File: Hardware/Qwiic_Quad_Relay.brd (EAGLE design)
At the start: 82.5 x 47 mm, 119 parts, among them J2 Qwiic Right Angle, J3 Qwiic Right Angle, J4 AVR_SPI_PROG_3X2TESTPOINTS, J9 POWER_JACK, K1 RELAY-SPDT-JZC-11F, K2 RELAY-SPDT-JZC-11F, K3 RELAY-SPDT-JZC-11F, K4 RELAY-SPDT-JZC-11F, Q1 600mA/40V, Q2 600mA/40V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

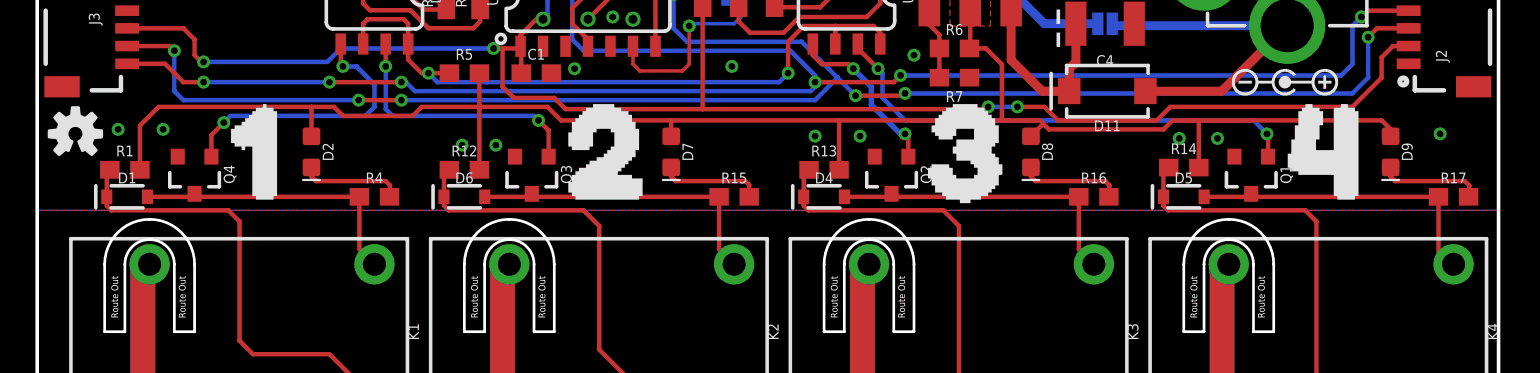
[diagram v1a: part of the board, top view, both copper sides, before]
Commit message: Moves 33 Ohm resistor to after the coil so that drop doesn't occur before it.
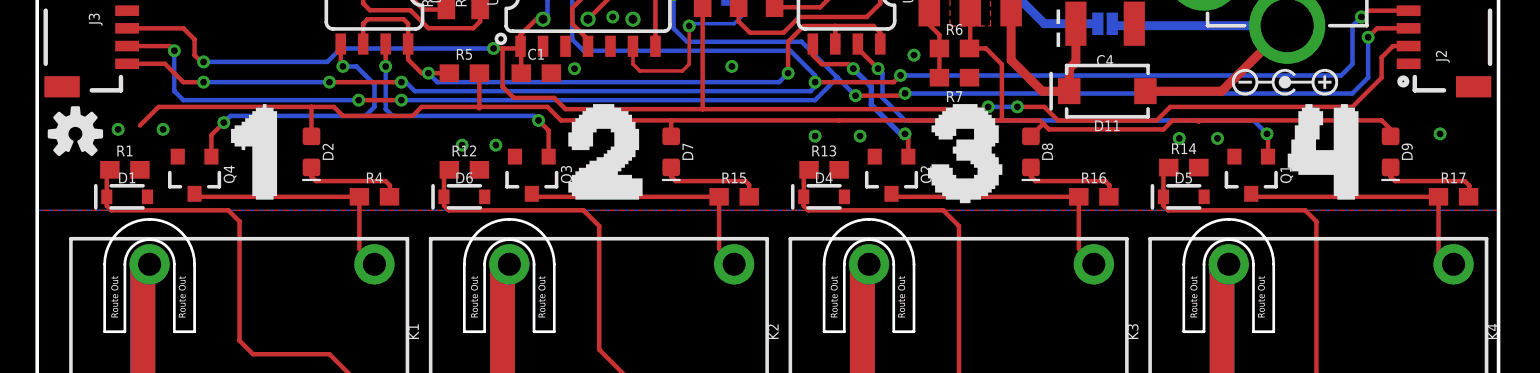
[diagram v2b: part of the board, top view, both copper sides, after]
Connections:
- removed net N$1: D6.C, K2.5, R12.1
- removed net N$14: D4.C, K3.5, R13.1
- removed net N$16: D5.C, K4.5, R14.1
- removed net N$7: D1.C, K1.5, R1.1
- new net N$10: D1.A, K1.1, R1.2
- new net N$18: D6.A, K2.1, R12.2
- new net N$23: D4.A, K3.1, R13.2
- new net N$24: D5.A, K4.1, R14.2
- net 5V: now also D1.C, D4.C, D5.C, D6.C, K1.5, K2.5, K3.5, K4.5; no longer R1.2, R12.2, R13.2, R14.2
- net N$12: now also R12.1; no longer D6.A, K2.1
- net N$15: now also R13.1; no longer D4.A, K3.1
- net N$17: now also R14.1; no longer D5.A, K4.1
- net N$2: now also R1.1; no longer D1.A, K1.1
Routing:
- net 5V: track 121.6 -> 217.8 mm
- net N$16: track 28.3 -> 0.00 mm
- net N$14: track 28.0 -> 0.00 mm
- net N$1: track 27.2 -> 0.00 mm
- net N$7: track 25.7 -> 0.00 mm
- net N$2: track 16.3 -> 12.6 mm
- net N$15: track 17.5 -> 13.9 mm
- net N$12: track 17.5 -> 13.9 mm
- net N$17: track 18.0 -> 14.7 mm

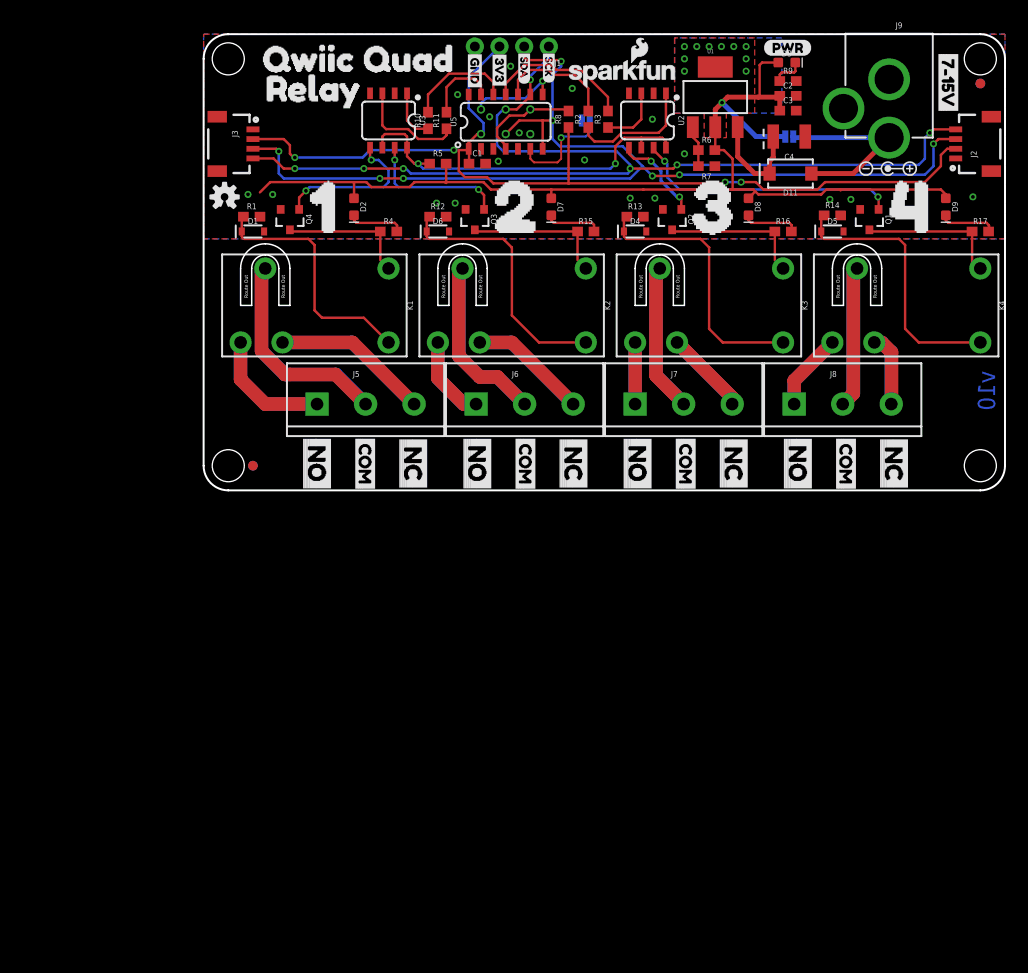
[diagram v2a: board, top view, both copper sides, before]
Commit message: Adds circuitry for DC-DC converter (no traces routed)
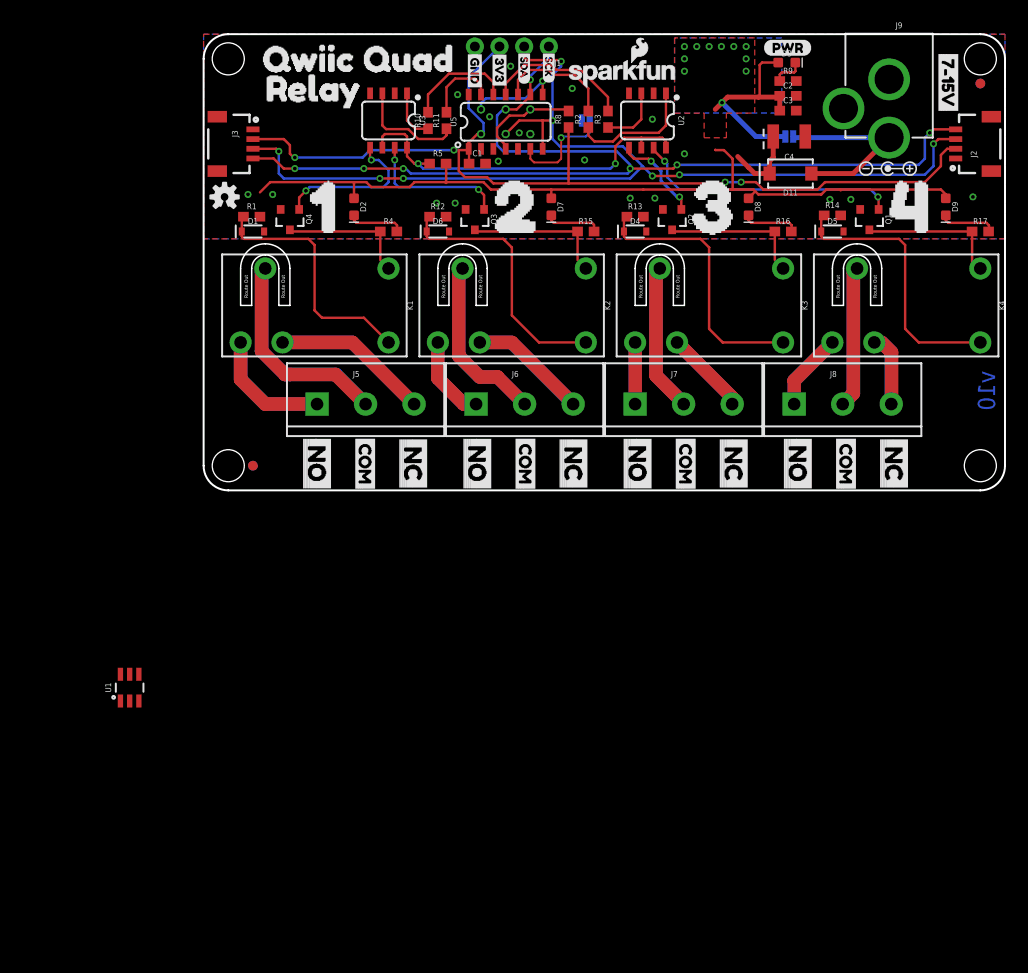
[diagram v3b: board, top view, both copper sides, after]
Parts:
- removed FRAME1: FRAME-LETTER, SparkFun-Aesthetics:CREATIVE_COMMONS
- removed R6: 240, SparkFun-Resistors:0603
- removed R7: 715, SparkFun-Resistors:0603
- added FRAME2: FRAME-LEDGER, SparkFun-Aesthetics:CREATIVE_COMMONS
- U1: value (none) -> LMR14010A; device SparkFun-IC-Power:SOT223 -> SparkFun-IC-Power:SOT23-6
- moved U1 85.7 mm to (-7.62, -20.3)
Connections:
- removed net N$19: R6.1, R7.2, U1.1
- new net SW: U1.6
- net 5V: no longer R6.2, U1.2, U1.4
- net GND: now also U1.2; no longer R7.1
- net N$4: no longer U1.3
- net VIN: now also U1.5
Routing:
- net N$19: track 4.25 -> 0.00 mm
- net 5V: track 217.8 -> 213.6 mm
- net N$4: track 11.0 -> 7.98 mm
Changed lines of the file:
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@@
 <attribute name="VALUE" value="BLUE" x="14.859" y="29.21" size="0.6096" layer="27" font="vector" ratio="20" rot="R270" align="top-center"/>
-</element>
-<element name="FRAME1" library="SparkFun-Aesthetics" package="CREATIVE_COMMONS" value="FRAME-LETTER" x="10.16" y="-16.51" smashed="yes">
-<attribute name="DESIGNER" value="" x="10.16" y="-16.51" size="1.778" layer="27" display="off"/>
-<attribute name="REV" value="" x="10.16" y="-16.51" size="1.778" layer="27" display="off"/>
 </element>
 <element name="J2" library="SparkFun-Connectors" package="1X04_1MM_RA" value="Qwiic Right Angle" x="77.47" y="35.687" smashed="yes" rot="R90">
@@
 <attribute name="PROD_ID" value="CONN-08197" x="70.612" y="50.038" size="1.778" layer="27" rot="R180" display="off"/>
 <attribute name="VALUE" x="72.3646" y="49.2252" size="0.6096" layer="27" font="vector" ratio="20" rot="R180"/>
-</element>
-<element name="U1" library="SparkFun-IC-Power" package="SOT223" value="" x="52.705" y="40.513" smashed="yes">
-<attribute name="NAME" x="51.8795" y="45.0215" size="0.4064" layer="25"/>
-<attribute name="PROD_ID" value="VREG-08170" x="52.705" y="40.513" size="1.778" layer="27" display="off"/>
-<attribute name="VALUE" x="51.6255" y="40.3225" size="0.4064" layer="27"/>
-</element>
-<element name="R6" library="SparkFun-Resistors" package="0603" value="240" x="51.816" y="35.052" smashed="yes">
-<attribute name="NAME" x="51.816" y="35.814" size="0.6096" layer="25" font="vector" ratio="20" align="bottom-center"/>
-<attribute name="PROD_ID" value="RES-07849" x="51.816" y="35.052" size="1.778" layer="27" display="off"/>
-<attribute name="VALUE" x="51.816" y="34.29" size="0.6096" layer="27" font="vector" ratio="20" align="top-center"/>
-</element>
-<element name="R7" library="SparkFun-Resistors" package="0603" value="715" x="51.816" y="33.401" smashed="yes" rot="R180">
-<attribute name="NAME" x="51.816" y="32.639" size="0.6096" layer="25" font="vector" ratio="20" rot="R180" align="bottom-center"/>
-<attribute name="PROD_ID" value="RES-07850" x="51.816" y="33.401" size="1.778" layer="27" rot="R180" display="off"/>
-<attribute name="VALUE" x="51.816" y="34.163" size="0.6096" layer="27" font="vector" ratio="20" rot="R180" align="top-center"/>
 </element>
 <element name="U$1" library="Labels" package="PWR-()-04" value="" x="57.658" y="45.593" smashed="yes"/>
@@
 <element name="U$10" library="Labels" package="3V3-03" value="" x="30.48" y="45.339" smashed="yes" rot="R270"/>
 <element name="U$12" library="Labels" package="3V3-03" value="" x="30.48" y="45.339" smashed="yes" rot="MR270"/>
+<element name="U1" library="SparkFun-IC-Power" package="SOT23-6" value="LMR14010A" x="-7.62" y="-20.32" smashed="yes">
+<attribute name="NAME" x="-9.525" y="-20.32" size="0.6096" layer="25" font="vector" ratio="20" rot="R90" align="bottom-center"/>
+<attribute name="PROD_ID" value="IC-15089" x="-7.62" y="-20.32" size="1.778" layer="27" display="off"/>
+<attribute name="VALUE" x="-5.08" y="-20.32" size="0.6096" layer="27" font="vector" ratio="20" rot="R90" align="bottom-center"/>
+</element>
+<element name="FRAME2" library="SparkFun-Aesthetics" package="CREATIVE_COMMONS" value="FRAME-LEDGER" x="10.16" y="-31.75" smashed="yes">
+<attribute name="DESIGNER" value="" x="10.16" y="-31.75" size="1.778" layer="27" display="off"/>
+<attribute name="REV" value="" x="10.16" y="-31.75" size="1.778" layer="27" display="off"/>
+</element>
 </elements>
 <signals>
@@
 <contactref element="J9" pad="GNDBREAK"/>
 <contactref element="J9" pad="GND"/>
-<contactref element="R7" pad="1"/>
 <via x="46.482" y="30.099" extent="1-16" drill="0.381"/>
 <via x="66.675" y="29.972" extent="1-16" drill="0.381"/>
@@
 <via x="26.162" y="40.767" extent="1-16" drill="0.381"/>
 <via x="32.512" y="36.83" extent="1-16" drill="0.381"/>
+<contactref element="U1" pad="2"/>
+<wire x1="7.94" y1="28.94" x2="-7.62" y2="-21.6951" width="0" layer="19" extent="1-1"/>
 </signal>
 <signal name="SDA/MOSI">
@@
 <wire x1="76.454" y1="30.087" x2="76.454" y2="30.48" width="0.254" layer="1"/>
 <wire x1="15.494" y1="30.087" x2="15.494" y2="31.75" width="0.254" layer="1"/>
-<contactref element="U1" pad="2"/>
-<contactref element="R6" pad="2"/>
 <contactref element="C2" pad="1"/>
 <contactref element="C3" pad="1"/>
 <wire x1="59.348" y1="39.116" x2="59.348" y2="40.64" width="0.508" layer="1"/>
-<wire x1="52.705" y1="37.4142" x2="52.705" y2="39.243" width="0.508" layer="1"/>
 <wire x1="52.705" y1="39.243" x2="53.4035" y2="39.9415" width="0.508" layer="1"/>
 <wire x1="53.4035" y1="39.9415" x2="53.975" y2="40.513" width="0.508" layer="1"/>
@@
 <wire x1="57.277" y1="43.815" x2="57.277" y2="40.64" width="0.254" layer="1"/>
 <wire x1="57.277" y1="40.64" x2="57.15" y2="40.513" width="0.254" layer="1"/>
-<wire x1="52.705" y1="37.4142" x2="52.705" y2="35.091" width="0.254" layer="1"/>
-<wire x1="52.705" y1="35.091" x2="52.666" y2="35.052" width="0.254" layer="1"/>
 <wire x1="54.495" y1="34.151" x2="53.594" y2="35.052" width="0.254" layer="1"/>
 <wire x1="52.744" y1="35.052" x2="52.705" y2="35.091" width="0.254" layer="1"/>
@@
 <wire x1="56.896" y1="36.449" x2="53.4035" y2="39.9415" width="0.508" layer="16"/>
 <via x="53.4035" y="39.9415" extent="1-16" drill="0.381"/>
-<contactref element="U1" pad="4"/>
 <polygon width="0.2032" layer="1" isolate="0.3048" thermals="no">
 <vertex x="48.514" y="46.609"/>
@@
 <wire x1="65.62" y1="30.9" x2="63.62" y2="28.021" width="0" layer="19" extent="1-1"/>
 <wire x1="3.93" y1="28.021" x2="5.803" y2="30.695" width="0" layer="19" extent="1-1"/>
+<wire x1="52.705" y1="39.243" x2="52.705" y2="35.091" width="0" layer="19" extent="1-1"/>
 <wire x1="22.98" y1="27.894" x2="24.98" y2="31.662" width="0" layer="19" extent="1-1"/>
 <wire x1="43.3" y1="27.894" x2="35.814" y2="30.087" width="0" layer="19" extent="1-1"/>
-</signal>
-<signal name="N$19">
-<contactref element="U1" pad="1"/>
-<contactref element="R6" pad="1"/>
-<contactref element="R7" pad="2"/>
-<wire x1="50.3936" y1="37.4142" x2="50.3936" y2="36.3864" width="0.254" layer="1"/>
-<wire x1="50.3936" y1="36.3864" x2="50.966" y2="35.814" width="0.254" layer="1"/>
-<wire x1="50.966" y1="33.401" x2="50.966" y2="35.052" width="0.254" layer="1"/>
-<wire x1="50.966" y1="35.814" x2="50.966" y2="35.052" width="0.254" layer="1"/>
 </signal>
 <signal name="VIN">
@@
 <wire x1="70.612" y1="36.338" x2="60.8424" y2="36.338" width="0.508" layer="16"/>
 <wire x1="60.8424" y1="36.338" x2="60.7314" y2="36.449" width="0.508" layer="16"/>
+<contactref element="U1" pad="5"/>
+<wire x1="-7.62" y1="-18.9449" x2="62.602" y2="32.639" width="0" layer="19" extent="1-1"/>
 </signal>
 <signal name="N$4">
-<contactref element="U1" pad="3"/>
 <contactref element="C4" pad="A"/>
 <contactref element="D11" pad="C"/>
-<wire x1="55.0164" y1="37.4142" x2="55.0164" y2="34.3916" width="0.508" layer="1"/>
 <wire x1="55.0164" y1="34.3916" x2="56.134" y2="33.274" width="0.508" layer="1"/>
 <wire x1="56.769" y1="32.639" x2="56.134" y2="33.274" width="0.508" layer="1"/>
@@
 <wire x1="65.62" y1="28.321" x2="65.92" y2="26.67" width="0" layer="19" extent="1-1"/>
 </signal>
+<signal name="SW">
+<contactref element="U1" pad="6"/>
+</signal>
 </signals>

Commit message: Re-adds dc-dc converter circuitry - somehow it was not in the last push
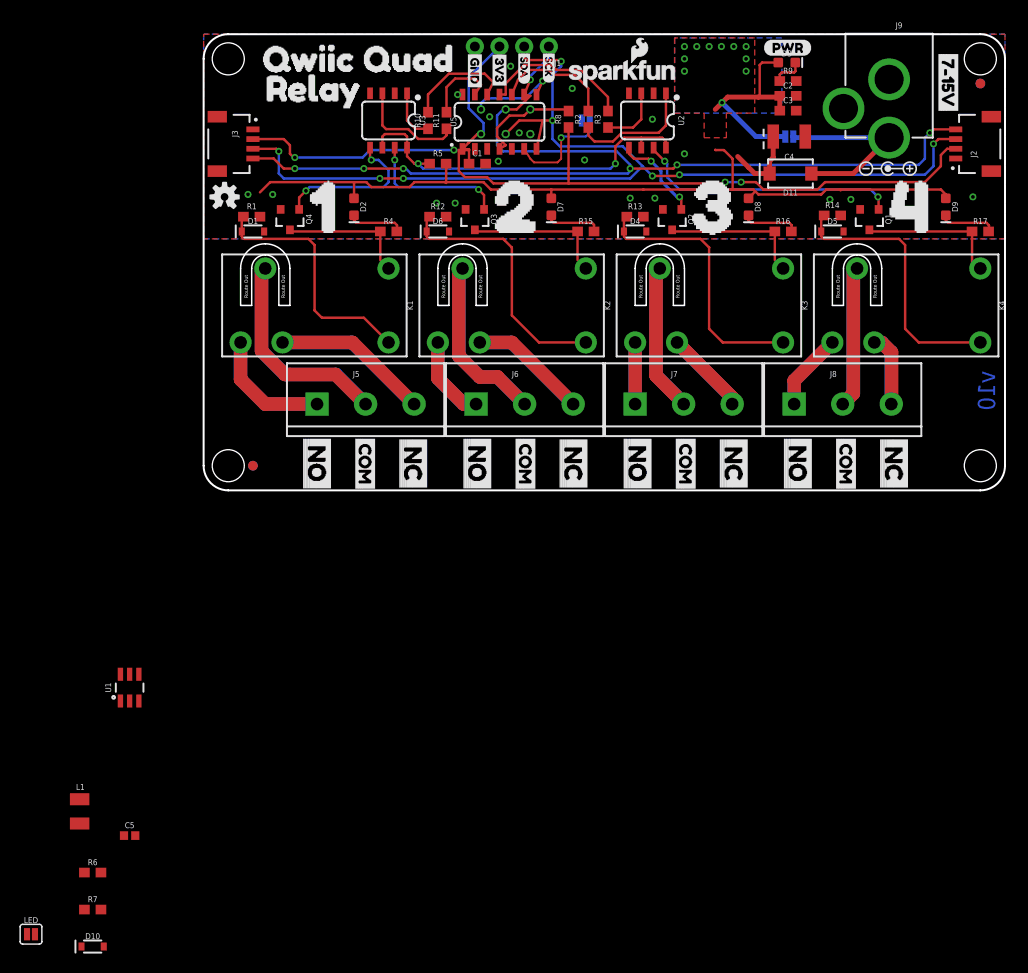
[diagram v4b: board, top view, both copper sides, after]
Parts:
- added C5: 0.1uF, SparkFun-Capacitors:0402
- added D10: 3A/10V/280mV, SparkFun-DiscreteSemi:SOD-323
- added L1: 15uH, SparkFun-Coils:INDUCTOR_LQH32
- added LED: JUMPER-SMT_2_NO_SILK, SparkFun-Jumpers:SMT-JUMPER_2_NO_SILK
- added R6: 20k, SparkFun-Resistors:0603
- added R7: 100k, SparkFun-Resistors:0603
- C3: value 0.1uF -> 10uF
- J2, J3: device SparkFun-Connectors:1X04_1MM_RA -> SparkFun-Connectors:JST04_1MM_RA
- renumbered JP10 to ADDR
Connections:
- removed net SW: U1.6
- new net N$1: C5.1, U1.1
- new net N$14: LED.2, R9.2
- new net N$16: R6.2, R7.1, U1.3
- new net N$7: C5.2, D10.C, L1.P$1, U1.6
- net 5V: now also L1.P$2, R7.2
- net GND: now also D10.A, LED.1, R6.1; no longer R9.2
- net N$4: now also U1.4, U1.5
- net VIN: no longer U1.5
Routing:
- net 3.3V: track 101.2 -> 102.0 mm
- net SCL/SCK: track 104.5 -> 105.1 mm
- net RELAY_CTRL2: track 15.3 -> 15.9 mm

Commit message: Routes new circuitry
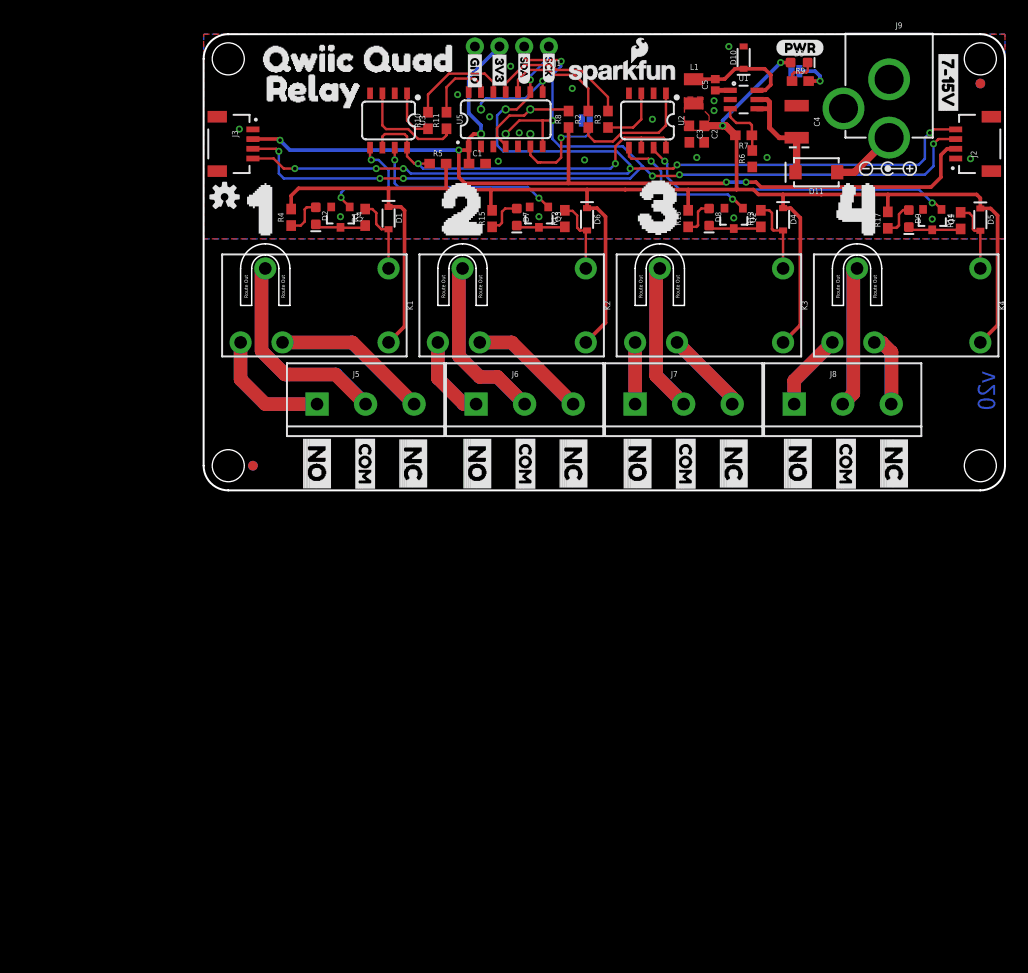
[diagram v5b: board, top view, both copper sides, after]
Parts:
- removed JP7: JUMPER-SMT_2_NO_SILK, SparkFun-Jumpers:SMT-JUMPER_2_NO_SILK
- moved LED 118.8 mm to (61.0, 43.2), flipped to the bottom, turned to 180 degrees
- moved D10 113.5 mm to (55.6, 44.6), turned to 90 degrees
- moved R7 104.2 mm to (55.6, 36.6), turned to 180 degrees
- moved R6 100.1 mm to (56.5, 34.2), turned to 90 degrees
- moved C5 98.1 mm to (52.7, 41.8), turned to 90 degrees
- moved L1 97.5 mm to (50.5, 41.1)
- moved U1 87.6 mm to (55.6, 40.3), turned to 270 degrees
- moved D6 15.4 mm to (39.5, 27.9), turned to 270 degrees
- moved D4 15.3 mm to (59.7, 27.9), turned to 270 degrees
- moved D5 15.3 mm to (80.0, 27.9), turned to 270 degrees
- moved D1 14.0 mm to (19.1, 28.0), turned to 270 degrees
- moved R14 13.2 mm to (78.0, 27.8), turned to 90 degrees
- moved R12 13.1 mm to (37.2, 28.0), turned to 90 degrees
- moved R13 13.0 mm to (57.4, 28.0), turned to 90 degrees
- moved R1 11.7 mm to (16.6, 28.1), turned to 90 degrees
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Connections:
- net N$1 renamed CB
- net N$16 renamed FB
- net N$4 renamed VIN_DC_DC
- net N$7 renamed SW
- removed net N$20: D9.C, R17.2
- removed net N$21: D8.C, R16.2
- removed net N$22: D7.C, R15.2
- new net N$1: D2.A, R4.1
- new net N$4: D7.A, R15.1
- new net N$7: D8.A, R16.1
- net 5V: now also R15.2, R16.2, R17.2, R4.2; no longer D2.A, D7.A, D8.A, D9.A, JP7.2
- net N$12: now also D7.C; no longer R15.1
- net N$15: now also D8.C; no longer R16.1
- net N$17: now also D9.C; no longer R17.1
- net N$2: now also D2.C; no longer R4.1
- net N$8: now also D9.A, R17.1; no longer D2.C, R4.2
- net VIN: no longer JP7.1
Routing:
- net 5V: track 213.4 -> 171.2 mm, vias 11 -> 2
- net VIN: track 19.5 -> 6.82 mm
- net SW: track 0.00 -> 11.3 mm
- net N$17: track 14.7 -> 5.49 mm
- net N$12: track 13.9 -> 5.05 mm
- net N$15: track 13.9 -> 5.54 mm
- net N$23: track 0.00 -> 8.03 mm
- net N$10: track 0.00 -> 7.98 mm
- net N$18: track 0.00 -> 7.83 mm
- net N$24: track 0.00 -> 7.44 mm
- net N$2: track 12.6 -> 5.80 mm
- net FB: track 0.00 -> 6.05 mm
- net OPTO_3: track 9.64 -> 15.6 mm
- net N$20: track 5.83 -> 0.00 mm
- net N$21: track 5.82 -> 0.00 mm
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- removed copper zone on layer 16, net 5V
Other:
- board text added: "v20"
- board text removed: "v10"
